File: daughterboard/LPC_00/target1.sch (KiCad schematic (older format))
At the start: 0 parts

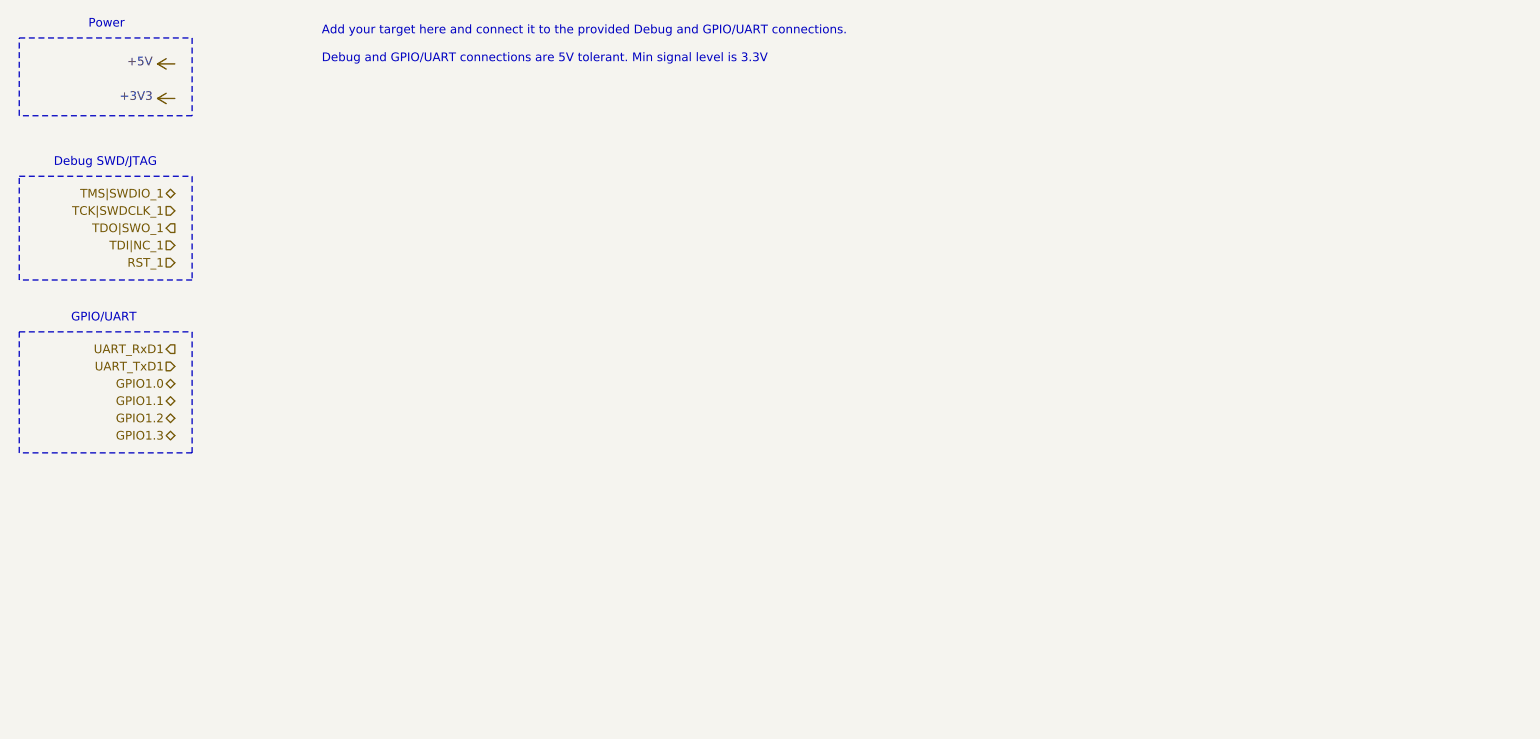
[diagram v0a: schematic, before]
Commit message: finished LPC Daughterboard schematics
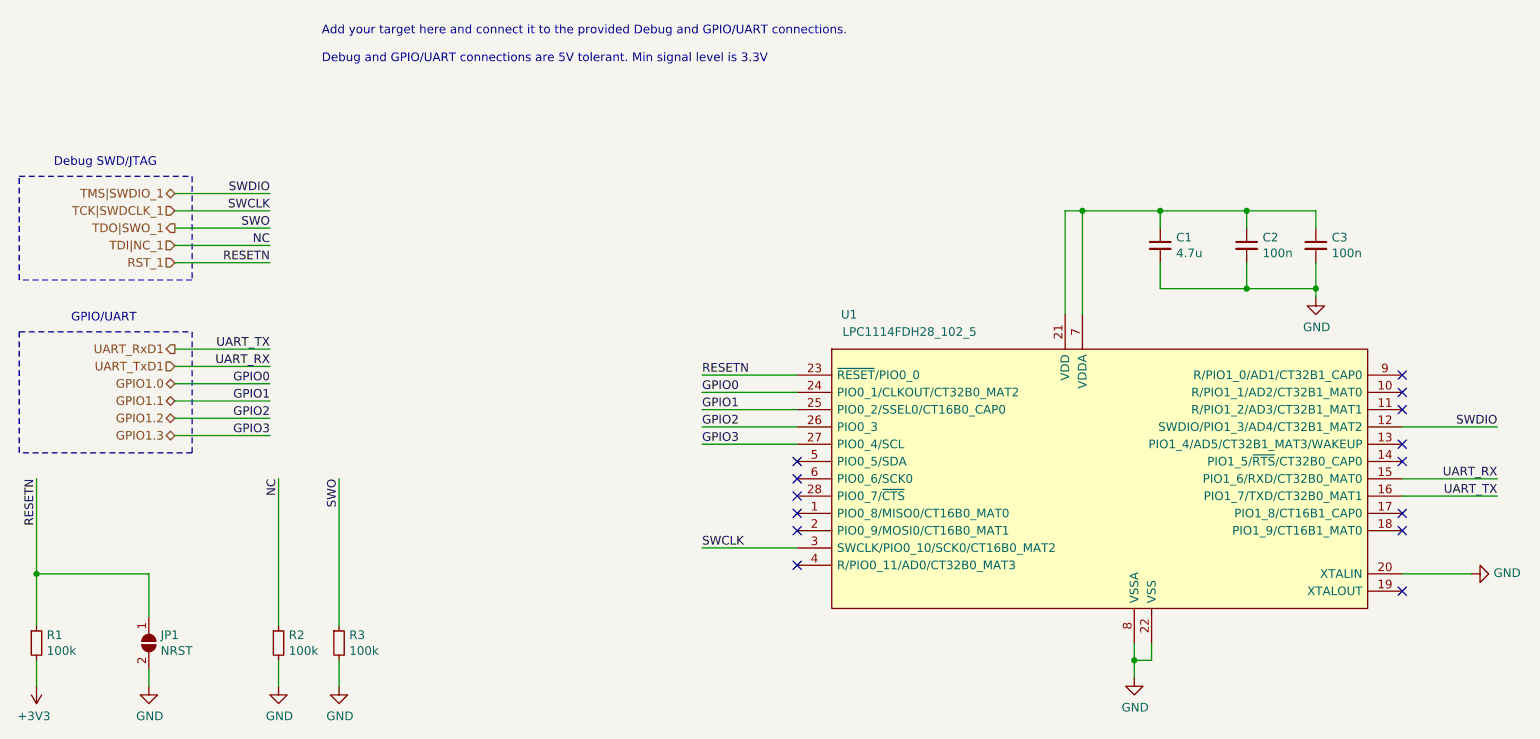
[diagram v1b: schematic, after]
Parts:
- added C1: 4.7u, symbol Device:C_Small
- added C2, C3: 100n, symbol Device:C_Small
- added JP1: NRST, symbol Jumper:SolderJumper_2_Open
- added R1, R2, R3: 100k, symbol Device:R_Small
- added U1: LPC1114FDH28_102_5, hive_daughterboard:LPC1114FDH28_1025, symbol hive_daughterboard:LPC1114FDH28_102_5
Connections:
- net +3V3: now also R1.2
- net GPIO1.0: now also U1.24 (PIO0_1/CLKOUT/CT32B0_MAT2)
- net GPIO1.1: now also U1.25 (PIO0_2/SSEL0/CT16B0_CAP0)
- net GPIO1.2: now also U1.26 (PIO0_3)
- net GPIO1.3: now also U1.27 (PIO0_4/SCL)
- net RST_1: now also JP1.1 (A), R1.1, U1.23 (~RESET~/PIO0_0)
- net TCK|SWDCLK_1: now also U1.3 (SWCLK/PIO0_10/SCK0/CT16B0_MAT2)
- net TDI|NC_1: now also R2.1
- net TDO|SWO_1: now also R3.1
- net TMS|SWDIO_1: now also U1.12 (SWDIO/PIO1_3/AD4/CT32B1_MAT2)
- net UART_RxD1: now also U1.16 (PIO1_7/TXD/CT32B0_MAT1)
- net UART_TxD1: now also U1.15 (PIO1_6/RXD/CT32B0_MAT0)
- new net: C1.1, C2.1, C3.1, U1.21 (VDD), U1.7 (VDDA)
- new net GND: C1.2, C2.2, C3.2, JP1.2 (B), R2.2, R3.2, U1.20 (XTALIN), U1.22 (VSS), U1.8 (VSSA)
- no-connect marks 0 -> 14
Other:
- note removed: "Power"
